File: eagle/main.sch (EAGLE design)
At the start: 24 parts, among them IC1 74LS595D, IC3 317EMP, IC4 74LS595D, Q1 BSS123, Q2 BSS123, Q3 BSS123, Q4 BSS123, Q5 BSS123

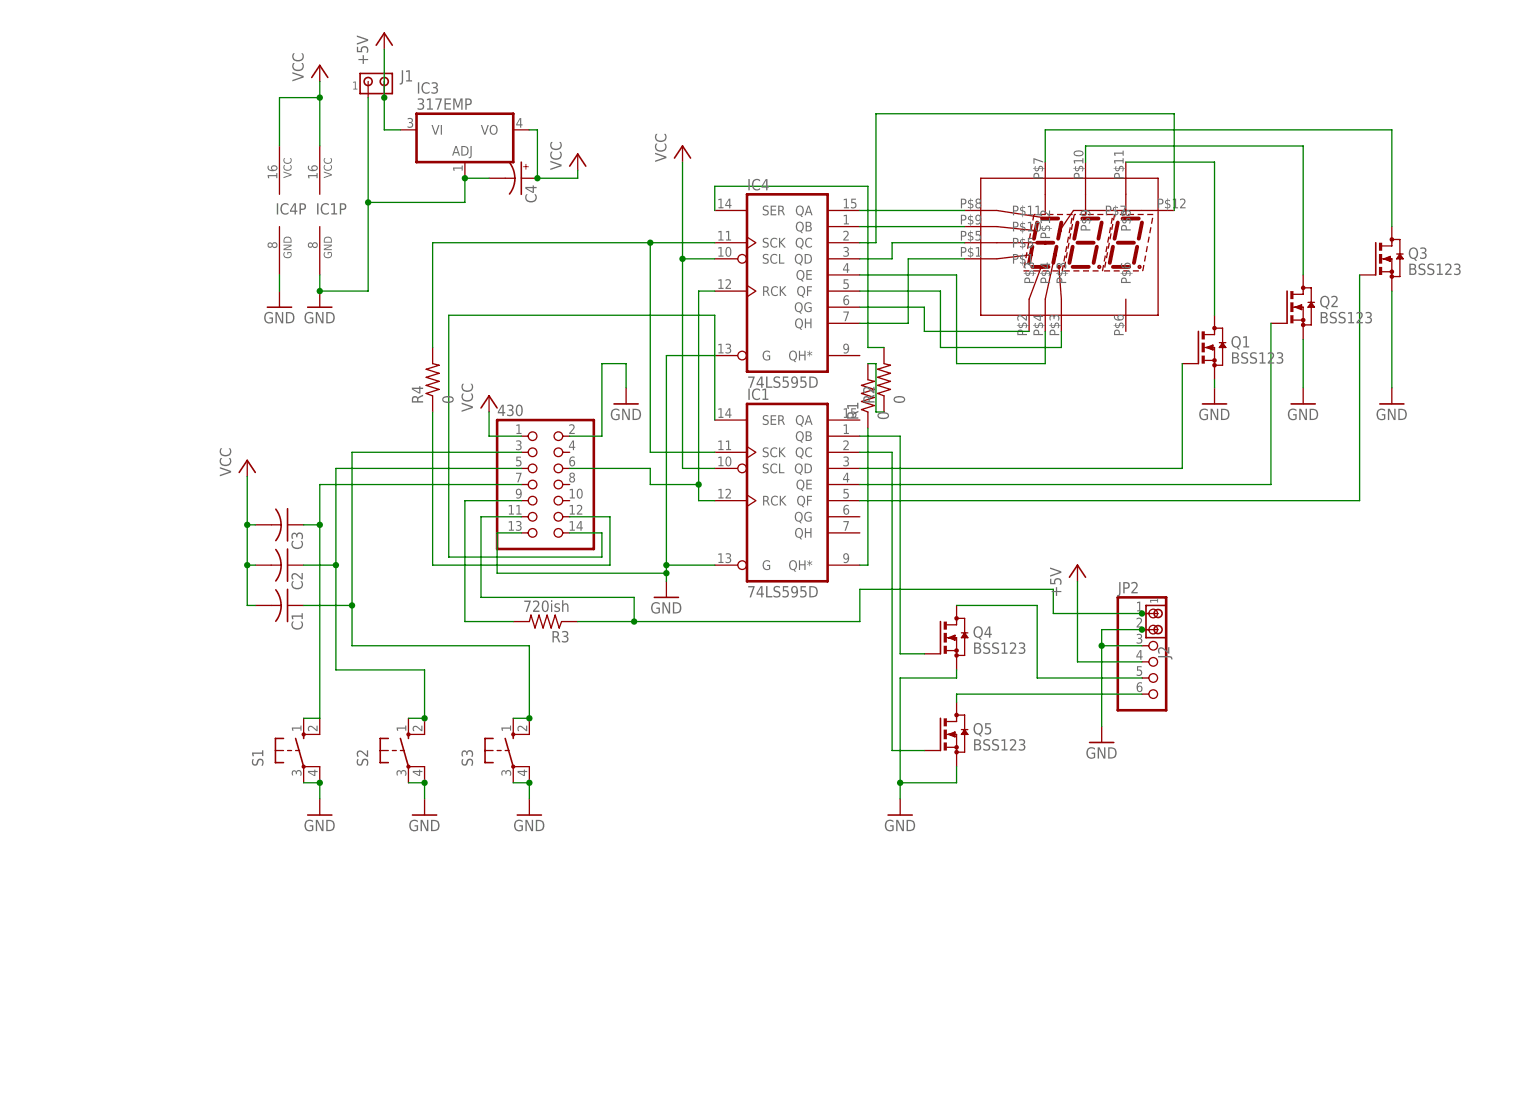
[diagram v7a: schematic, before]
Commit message: Temperature control is working.
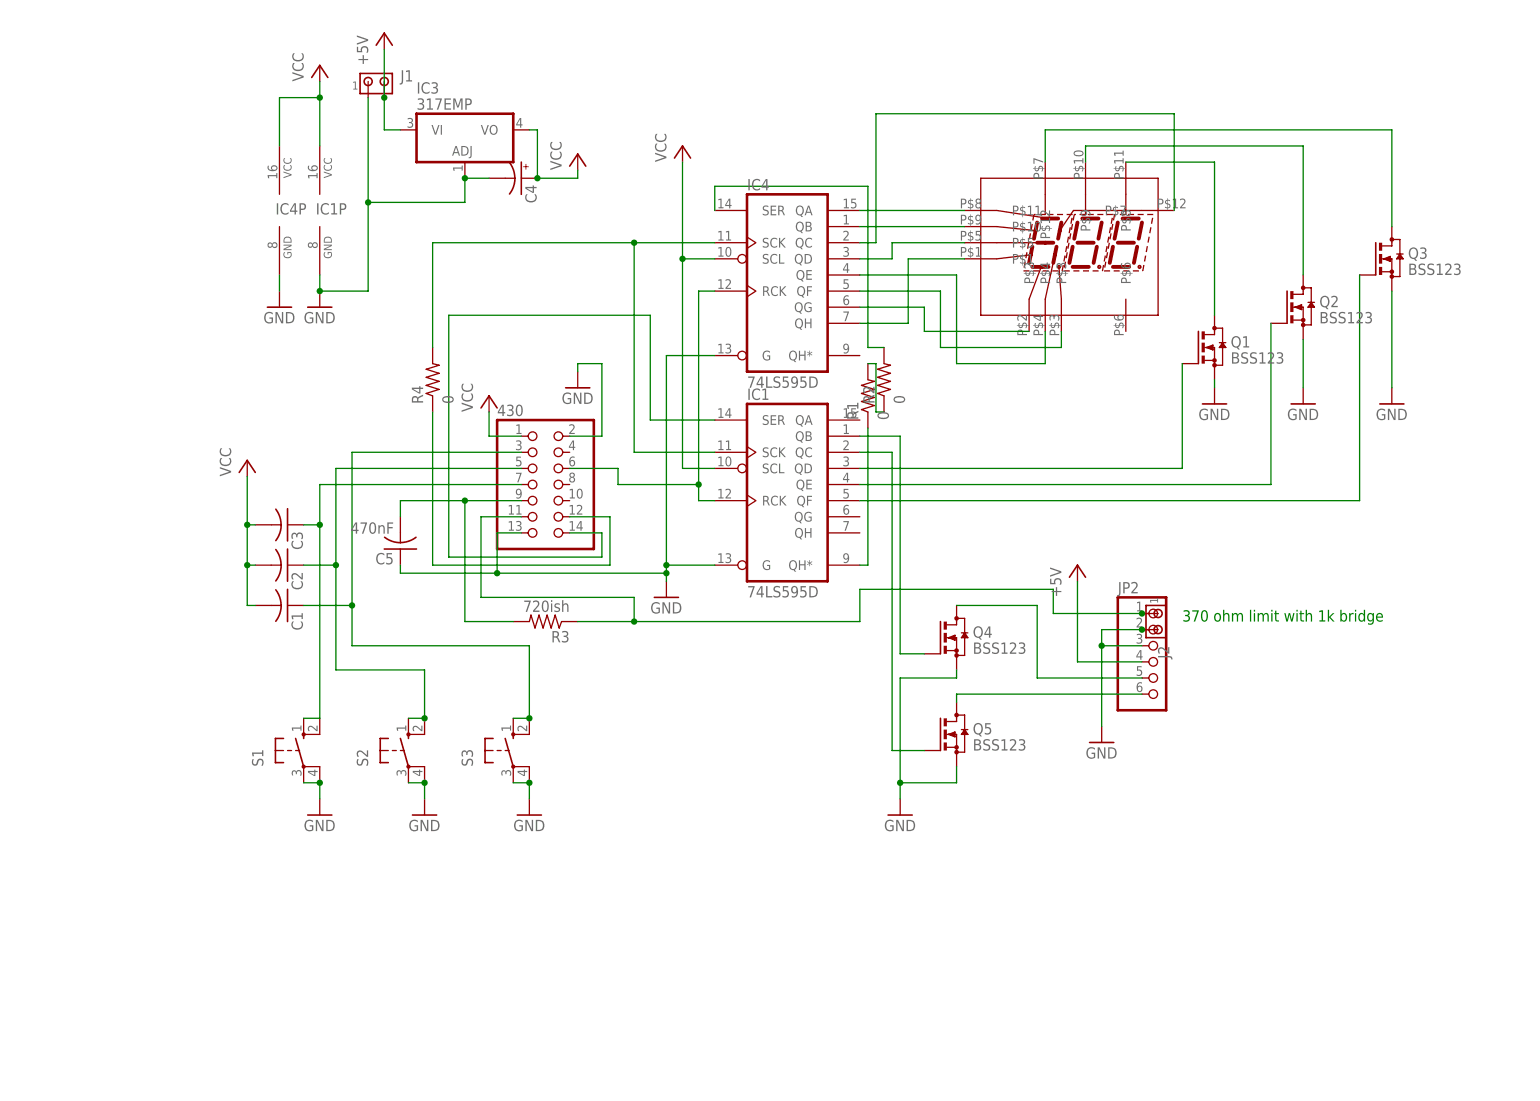
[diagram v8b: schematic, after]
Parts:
- added C5: 470nF, rcl:C-USC0603K
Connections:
- net GND: now also C5.1
- net N$31: now also C5.2
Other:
- note added: "370 ohm limit with 1k bridge"
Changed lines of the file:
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@@
 <grid distance="0.05" unitdist="inch" unit="inch" style="lines" multiple="1" display="no" altdistance="0.01" altunitdist="inch" altunit="inch"/>
 <layers>
-<layer number="1" name="Top" color="4" fill="1" visible="yes" active="no"/>
-<layer number="16" name="Bottom" color="1" fill="1" visible="yes" active="no"/>
-<layer number="17" name="Pads" color="2" fill="1" visible="yes" active="no"/>
-<layer number="18" name="Vias" color="2" fill="1" visible="yes" active="no"/>
-<layer number="19" name="Unrouted" color="6" fill="1" visible="yes" active="no"/>
-<layer number="20" name="Dimension" color="15" fill="1" visible="yes" active="no"/>
-<layer number="21" name="tPlace" color="7" fill="1" visible="yes" active="no"/>
-<layer number="22" name="bPlace" color="7" fill="1" visible="yes" active="no"/>
-<layer number="23" name="tOrigins" color="15" fill="1" visible="yes" active="no"/>
-<layer number="24" name="bOrigins" color="15" fill="1" visible="yes" active="no"/>
-<layer number="25" name="tNames" color="7" fill="1" visible="yes" active="no"/>
-<layer number="26" name="bNames" color="7" fill="1" visible="yes" active="no"/>
-<layer number="27" name="tValues" color="7" fill="1" visible="yes" active="no"/>
-<layer number="28" name="bValues" color="7" fill="1" visible="yes" active="no"/>
+<layer number="1" name="Top" color="4" fill="1" visible="no" active="no"/>
+<layer number="16" name="Bottom" color="1" fill="1" visible="no" active="no"/>
+<layer number="17" name="Pads" color="2" fill="1" visible="no" active="no"/>
+<layer number="18" name="Vias" color="2" fill="1" visible="no" active="no"/>
+<layer number="19" name="Unrouted" color="6" fill="1" visible="no" active="no"/>
+<layer number="20" name="Dimension" color="15" fill="1" visible="no" active="no"/>
+<layer number="21" name="tPlace" color="7" fill="1" visible="no" active="no"/>
+<layer number="22" name="bPlace" color="7" fill="1" visible="no" active="no"/>
+<layer number="23" name="tOrigins" color="15" fill="1" visible="no" active="no"/>
+<layer number="24" name="bOrigins" color="15" fill="1" visible="no" active="no"/>
+<layer number="25" name="tNames" color="7" fill="1" visible="no" active="no"/>
+<layer number="26" name="bNames" color="7" fill="1" visible="no" active="no"/>
+<layer number="27" name="tValues" color="7" fill="1" visible="no" active="no"/>
+<layer number="28" name="bValues" color="7" fill="1" visible="no" active="no"/>
 <layer number="29" name="tStop" color="7" fill="3" visible="no" active="no"/>
 <layer number="30" name="bStop" color="7" fill="6" visible="no" active="no"/>
@@
 <layer number="35" name="tGlue" color="7" fill="4" visible="no" active="no"/>
 <layer number="36" name="bGlue" color="7" fill="5" visible="no" active="no"/>
-<layer number="37" name="tTest" color="7" fill="1" visible="yes" active="no"/>
-<layer number="38" name="bTest" color="7" fill="1" visible="yes" active="no"/>
+<layer number="37" name="tTest" color="7" fill="1" visible="no" active="no"/>
+<layer number="38" name="bTest" color="7" fill="1" visible="no" active="no"/>
 <layer number="39" name="tKeepout" color="4" fill="11" visible="no" active="no"/>
 <layer number="40" name="bKeepout" color="1" fill="11" visible="no" active="no"/>
@@
 <layer number="44" name="Drills" color="7" fill="1" visible="no" active="no"/>
 <layer number="45" name="Holes" color="7" fill="1" visible="no" active="no"/>
-<layer number="46" name="Milling" color="3" fill="1" visible="yes" active="no"/>
-<layer number="47" name="Measures" color="7" fill="1" visible="yes" active="no"/>
-<layer number="48" name="Document" color="7" fill="1" visible="yes" active="no"/>
-<layer number="49" name="Reference" color="7" fill="1" visible="yes" active="no"/>
-<layer number="50" name="dxf" color="7" fill="1" visible="yes" active="no"/>
-<layer number="51" name="tDocu" color="7" fill="1" visible="yes" active="no"/>
-<layer number="52" name="bDocu" color="7" fill="1" visible="yes" active="no"/>
-<layer number="53" name="tGND_GNDA" color="7" fill="9" visible="yes" active="no"/>
-<layer number="54" name="bGND_GNDA" color="1" fill="9" visible="yes" active="no"/>
-<layer number="56" name="wert" color="7" fill="1" visible="yes" active="no"/>
+<layer number="46" name="Milling" color="3" fill="1" visible="no" active="no"/>
+<layer number="47" name="Measures" color="7" fill="1" visible="no" active="no"/>
+<layer number="48" name="Document" color="7" fill="1" visible="no" active="no"/>
+<layer number="49" name="Reference" color="7" fill="1" visible="no" active="no"/>
+<layer number="50" name="dxf" color="7" fill="1" visible="no" active="no"/>
+<layer number="51" name="tDocu" color="7" fill="1" visible="no" active="no"/>
+<layer number="52" name="bDocu" color="7" fill="1" visible="no" active="no"/>
+<layer number="53" name="tGND_GNDA" color="7" fill="9" visible="no" active="no"/>
+<layer number="54" name="bGND_GNDA" color="1" fill="9" visible="no" active="no"/>
+<layer number="56" name="wert" color="7" fill="1" visible="no" active="no"/>
 <layer number="91" name="Nets" color="2" fill="1" visible="yes" active="yes"/>
 <layer number="92" name="Busses" color="1" fill="1" visible="yes" active="yes"/>
@@
 <part name="P+6" library="supply1" deviceset="VCC" device=""/>
 <part name="J2" library="con-amp" deviceset="MTA02-100" device=""/>
+<part name="C5" library="rcl" deviceset="C-US" device="C0603K" value="470nF"/>
 </parts>
 <sheets>
 <sheet>
 <plain>
+<text x="175.26" y="29.21" size="1.778" layer="91">370 ohm limit with 1k bridge</text>
 </plain>
 <instances>
 <instance part="430" gate="A" x="73.66" y="50.8"/>
 <instance part="U$1" gate="G$1" x="160.02" y="88.9"/>
-<instance part="GND1" gate="1" x="87.63" y="63.5"/>
+<instance part="GND1" gate="1" x="80.01" y="66.04"/>
 <instance part="R3" gate="G$1" x="74.93" y="29.21" rot="R180"/>
 <instance part="GND2" gate="1" x="162.56" y="10.16"/>
@@
 <instance part="P+6" gate="VCC" x="39.37" y="116.84"/>
 <instance part="J2" gate="G$1" x="171.45" y="30.48" rot="R270"/>
+<instance part="C5" gate="G$1" x="52.07" y="40.64" rot="R180"/>
 </instances>
 <busses>
@@
 <wire x1="83.82" y1="58.42" x2="83.82" y2="69.85" width="0.1524" layer="91"/>
 <pinref part="GND1" gate="1" pin="GND"/>
-<wire x1="83.82" y1="69.85" x2="87.63" y2="69.85" width="0.1524" layer="91"/>
-<wire x1="87.63" y1="69.85" x2="87.63" y2="66.04" width="0.1524" layer="91"/>
+<wire x1="83.82" y1="69.85" x2="80.01" y2="69.85" width="0.1524" layer="91"/>
+<wire x1="80.01" y1="69.85" x2="80.01" y2="68.58" width="0.1524" layer="91"/>
 </segment>
 <segment>
@@
 <junction x="93.98" y="36.83"/>
 <junction x="93.98" y="38.1"/>
+<pinref part="C5" gate="G$1" pin="1"/>
+<wire x1="52.07" y1="38.1" x2="52.07" y2="36.83" width="0.1524" layer="91"/>
+<wire x1="52.07" y1="36.83" x2="67.31" y2="36.83" width="0.1524" layer="91"/>
+<junction x="67.31" y="36.83"/>
 </segment>
 </net>
@@
 <wire x1="59.69" y1="77.47" x2="59.69" y2="39.37" width="0.1524" layer="91"/>
 <pinref part="IC1" gate="A" pin="SER"/>
-<wire x1="101.6" y1="60.96" x2="101.6" y2="77.47" width="0.1524" layer="91"/>
-<wire x1="101.6" y1="77.47" x2="59.69" y2="77.47" width="0.1524" layer="91"/>
+<wire x1="101.6" y1="60.96" x2="91.44" y2="60.96" width="0.1524" layer="91"/>
+<wire x1="91.44" y1="60.96" x2="91.44" y2="77.47" width="0.1524" layer="91"/>
+<wire x1="91.44" y1="77.47" x2="59.69" y2="77.47" width="0.1524" layer="91"/>
 <wire x1="59.69" y1="39.37" x2="83.82" y2="39.37" width="0.1524" layer="91"/>
 <wire x1="83.82" y1="39.37" x2="83.82" y2="43.18" width="0.1524" layer="91"/>
@@
 <segment>
 <pinref part="IC1" gate="A" pin="SCK"/>
-<wire x1="91.44" y1="55.88" x2="101.6" y2="55.88" width="0.1524" layer="91"/>
+<wire x1="88.9" y1="55.88" x2="101.6" y2="55.88" width="0.1524" layer="91"/>
 <pinref part="IC4" gate="A" pin="SCK"/>
-<wire x1="101.6" y1="88.9" x2="91.44" y2="88.9" width="0.1524" layer="91"/>
-<wire x1="91.44" y1="88.9" x2="57.15" y2="88.9" width="0.1524" layer="91"/>
+<wire x1="101.6" y1="88.9" x2="88.9" y2="88.9" width="0.1524" layer="91"/>
+<wire x1="88.9" y1="88.9" x2="57.15" y2="88.9" width="0.1524" layer="91"/>
 <wire x1="57.15" y1="88.9" x2="57.15" y2="72.39" width="0.1524" layer="91"/>
-<wire x1="91.44" y1="88.9" x2="91.44" y2="55.88" width="0.1524" layer="91"/>
-<junction x="91.44" y="88.9"/>
+<wire x1="88.9" y1="88.9" x2="88.9" y2="55.88" width="0.1524" layer="91"/>
+<junction x="88.9" y="88.9"/>
 <pinref part="R4" gate="G$1" pin="2"/>
 </segment>
@@
 <wire x1="99.06" y1="48.26" x2="101.6" y2="48.26" width="0.1524" layer="91"/>
 <pinref part="430" gate="A" pin="6"/>
-<wire x1="78.74" y1="53.34" x2="91.44" y2="53.34" width="0.1524" layer="91"/>
-<wire x1="91.44" y1="53.34" x2="91.44" y2="50.8" width="0.1524" layer="91"/>
-<wire x1="91.44" y1="50.8" x2="99.06" y2="50.8" width="0.1524" layer="91"/>
+<wire x1="78.74" y1="53.34" x2="86.36" y2="53.34" width="0.1524" layer="91"/>
+<wire x1="86.36" y1="53.34" x2="86.36" y2="50.8" width="0.1524" layer="91"/>
+<wire x1="86.36" y1="50.8" x2="99.06" y2="50.8" width="0.1524" layer="91"/>
 <junction x="99.06" y="50.8"/>
 </segment>
@@
 <wire x1="62.23" y1="29.21" x2="69.85" y2="29.21" width="0.1524" layer="91"/>
 <pinref part="R3" gate="G$1" pin="2"/>
-</segment>
-</net>
+<wire x1="62.23" y1="48.26" x2="52.07" y2="48.26" width="0.1524" layer="91"/>
+<junction x="62.23" y="48.26"/>
+<pinref part="C5" gate="G$1" pin="2"/>
+<wire x1="52.07" y1="48.26" x2="52.07" y2="45.72" width="0.1524" layer="91"/>
+</segment>
+</net>
